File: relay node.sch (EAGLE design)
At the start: 25 parts, among them J1 Channels, J2 LED, J3 PROG, J4 AUX, U1 ESP-WROOM-02U, U2 MCP23018-E/SS, U3 TLV75533

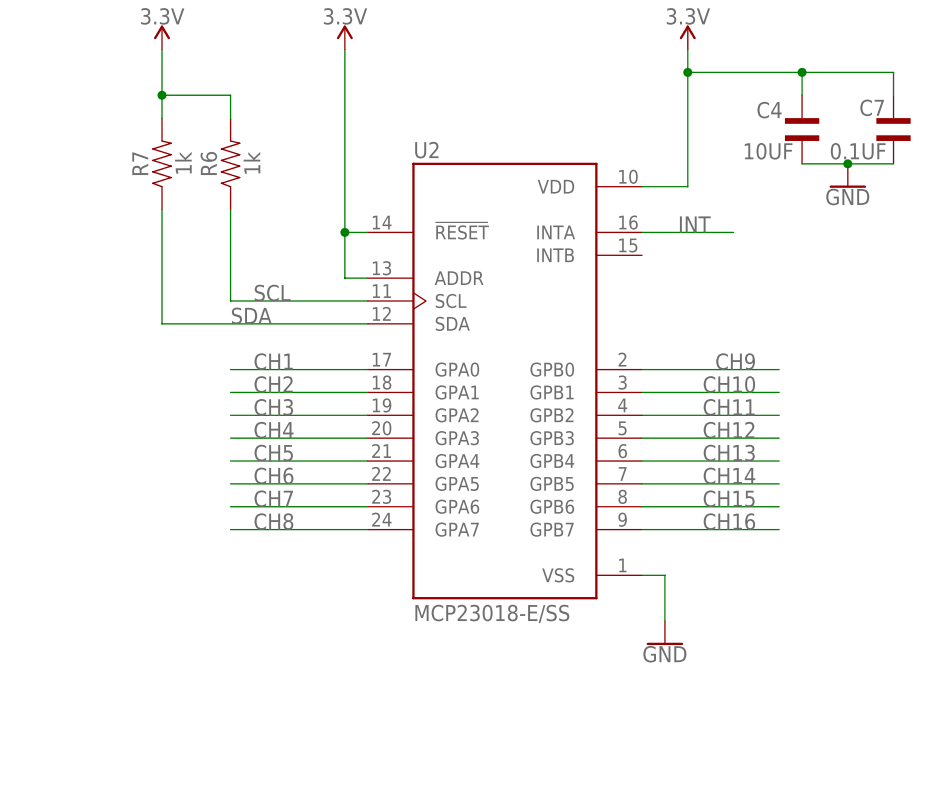
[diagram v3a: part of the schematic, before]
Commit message: Replace I/O expander to MCP23018 28-SOIC Replace BOM part numbers to match JLCPB inventory
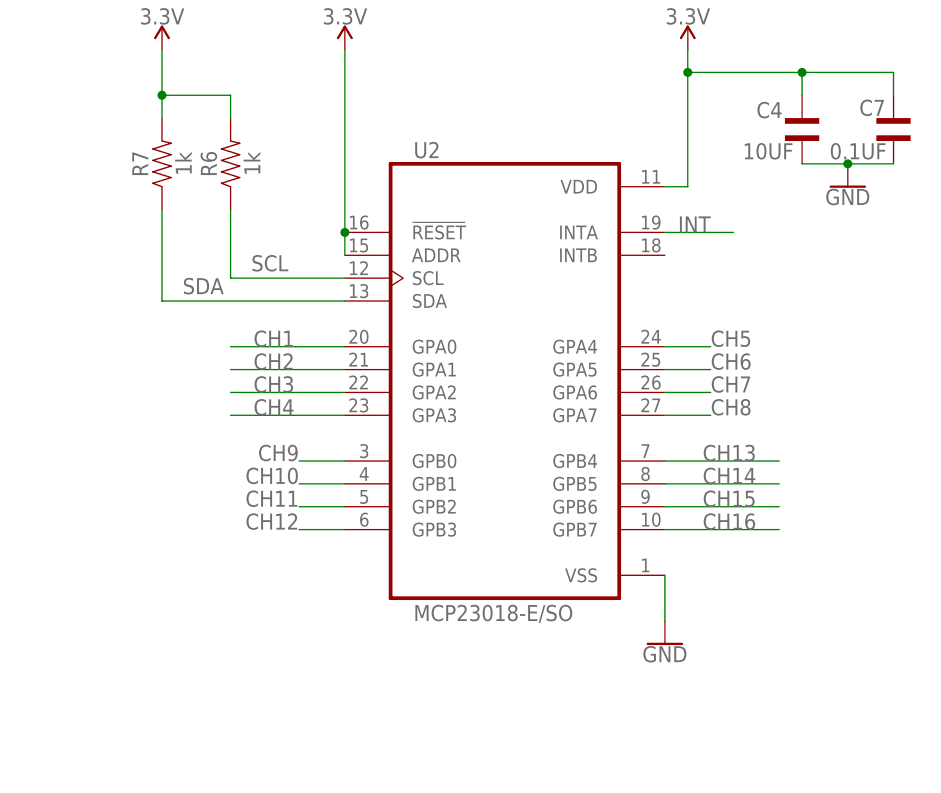
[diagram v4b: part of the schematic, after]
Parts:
- U2: value MCP23018-E/SS -> MCP23018-E/SO; device SFM-Project:MCP23018-E/SS -> SFM-Project:MCP23018-E/SO
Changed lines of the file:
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@@
 <part name="R7" library="SFM-Project" deviceset="1KOHM" device="-0603-1/10W-5%" value="1k"/>
 <part name="SUPPLY6" library="SparkFun-PowerSymbols" deviceset="3.3V" device=""/>
-<part name="U2" library="SFM-Project" deviceset="MCP23018-E/SS" device=""/>
+<part name="U2" library="SFM-Project" deviceset="MCP23018-E/SO" device=""/>
 <part name="SUPPLY7" library="SparkFun-PowerSymbols" deviceset="3.3V" device=""/>
 <part name="U1" library="SFM-Project" deviceset="ESP-WROOM-02U" device=""/>
@@
 <wire x1="180.34" y1="154.94" x2="180.34" y2="152.4" width="0.1524" layer="91"/>
 <wire x1="180.34" y1="152.4" x2="180.34" y2="139.7" width="0.1524" layer="91"/>
-<wire x1="180.34" y1="139.7" x2="175.26" y2="139.7" width="0.1524" layer="91"/>
+<wire x1="180.34" y1="139.7" x2="177.8" y2="139.7" width="0.1524" layer="91"/>
 <pinref part="C4" gate="G$1" pin="1"/>
 <wire x1="193.04" y1="149.86" x2="193.04" y2="152.4" width="0.1524" layer="91"/>
@@
 <pinref part="U2" gate="G$1" pin="ADDR"/>
 <pinref part="SUPPLY7" gate="G$1" pin="3.3V"/>
-<wire x1="144.78" y1="129.54" x2="142.24" y2="129.54" width="0.1524" layer="91"/>
-<wire x1="142.24" y1="129.54" x2="142.24" y2="134.62" width="0.1524" layer="91"/>
+<wire x1="142.24" y1="132.08" x2="142.24" y2="134.62" width="0.1524" layer="91"/>
 <pinref part="U2" gate="G$1" pin="!RESET"/>
 <wire x1="142.24" y1="134.62" x2="142.24" y2="154.94" width="0.1524" layer="91"/>
-<wire x1="144.78" y1="134.62" x2="142.24" y2="134.62" width="0.1524" layer="91"/>
 <junction x="142.24" y="134.62"/>
 </segment>
@@
 <pinref part="U2" gate="G$1" pin="VSS"/>
 <pinref part="GND4" gate="1" pin="GND"/>
-<wire x1="175.26" y1="96.52" x2="177.8" y2="96.52" width="0.1524" layer="91"/>
 <wire x1="177.8" y1="96.52" x2="177.8" y2="91.44" width="0.1524" layer="91"/>
 </segment>
@@
 <segment>
 <pinref part="U2" gate="G$1" pin="GPA0"/>
-<wire x1="144.78" y1="119.38" x2="129.54" y2="119.38" width="0.1524" layer="91"/>
-<label x="132.08" y="119.38" size="1.778" layer="95"/>
+<wire x1="142.24" y1="121.92" x2="129.54" y2="121.92" width="0.1524" layer="91"/>
+<label x="132.08" y="121.92" size="1.778" layer="95"/>
 </segment>
 <segment>
@@
 <segment>
 <pinref part="U2" gate="G$1" pin="GPA1"/>
-<wire x1="144.78" y1="116.84" x2="129.54" y2="116.84" width="0.1524" layer="91"/>
-<label x="132.08" y="116.84" size="1.778" layer="95"/>
+<wire x1="142.24" y1="119.38" x2="129.54" y2="119.38" width="0.1524" layer="91"/>
+<label x="132.08" y="119.38" size="1.778" layer="95"/>
 </segment>
 <segment>
@@
 <segment>
 <pinref part="U2" gate="G$1" pin="GPA2"/>
-<wire x1="144.78" y1="114.3" x2="129.54" y2="114.3" width="0.1524" layer="91"/>
-<label x="132.08" y="114.3" size="1.778" layer="95"/>
+<wire x1="142.24" y1="116.84" x2="129.54" y2="116.84" width="0.1524" layer="91"/>
+<label x="132.08" y="116.84" size="1.778" layer="95"/>
 </segment>
 <segment>
@@
 <segment>
 <pinref part="U2" gate="G$1" pin="GPA3"/>
-<wire x1="144.78" y1="111.76" x2="129.54" y2="111.76" width="0.1524" layer="91"/>
-<label x="132.08" y="111.76" size="1.778" layer="95"/>
+<wire x1="142.24" y1="114.3" x2="129.54" y2="114.3" width="0.1524" layer="91"/>
+<label x="132.08" y="114.3" size="1.778" layer="95"/>
 </segment>
 <segment>
@@
 <segment>
 <pinref part="U2" gate="G$1" pin="GPA4"/>
-<wire x1="144.78" y1="109.22" x2="129.54" y2="109.22" width="0.1524" layer="91"/>
-<label x="132.08" y="109.22" size="1.778" layer="95"/>
+<wire x1="177.8" y1="121.92" x2="182.88" y2="121.92" width="0.1524" layer="91"/>
+<label x="182.88" y="121.92" size="1.778" layer="95"/>
 </segment>
 <segment>
@@
 <segment>
 <pinref part="U2" gate="G$1" pin="GPA5"/>
-<wire x1="144.78" y1="106.68" x2="129.54" y2="106.68" width="0.1524" layer="91"/>
-<label x="132.08" y="106.68" size="1.778" layer="95"/>
+<wire x1="177.8" y1="119.38" x2="182.88" y2="119.38" width="0.1524" layer="91"/>
+<label x="182.88" y="119.38" size="1.778" layer="95"/>
 </segment>
 <segment>
@@
 <segment>
 <pinref part="U2" gate="G$1" pin="GPA6"/>
-<wire x1="144.78" y1="104.14" x2="129.54" y2="104.14" width="0.1524" layer="91"/>
-<label x="132.08" y="104.14" size="1.778" layer="95"/>
+<wire x1="177.8" y1="116.84" x2="182.88" y2="116.84" width="0.1524" layer="91"/>
+<label x="182.88" y="116.84" size="1.778" layer="95"/>
 </segment>
 <segment>
@@
 <segment>
 <pinref part="U2" gate="G$1" pin="GPA7"/>
-<wire x1="144.78" y1="101.6" x2="129.54" y2="101.6" width="0.1524" layer="91"/>
-<label x="132.08" y="101.6" size="1.778" layer="95"/>
+<wire x1="177.8" y1="114.3" x2="182.88" y2="114.3" width="0.1524" layer="91"/>
+<label x="182.88" y="114.3" size="1.778" layer="95"/>
 </segment>
 <segment>
@@
 <segment>
 <pinref part="U2" gate="G$1" pin="GPB0"/>
-<wire x1="175.26" y1="119.38" x2="190.5" y2="119.38" width="0.1524" layer="91"/>
-<label x="187.96" y="119.38" size="1.778" layer="95" align="bottom-right"/>
+<wire x1="142.24" y1="109.22" x2="137.16" y2="109.22" width="0.1524" layer="91"/>
+<label x="137.16" y="109.22" size="1.778" layer="95" align="bottom-right"/>
 </segment>
 <segment>
@@
 <segment>
 <pinref part="U2" gate="G$1" pin="GPB1"/>
-<wire x1="175.26" y1="116.84" x2="190.5" y2="116.84" width="0.1524" layer="91"/>
-<label x="187.96" y="116.84" size="1.778" layer="95" align="bottom-right"/>
+<wire x1="142.24" y1="106.68" x2="137.16" y2="106.68" width="0.1524" layer="91"/>
+<label x="137.16" y="106.68" size="1.778" layer="95" align="bottom-right"/>
 </segment>
 <segment>
@@
 <segment>
 <pinref part="U2" gate="G$1" pin="GPB2"/>
-<wire x1="175.26" y1="114.3" x2="190.5" y2="114.3" width="0.1524" layer="91"/>
-<label x="187.96" y="114.3" size="1.778" layer="95" align="bottom-right"/>
+<wire x1="142.24" y1="104.14" x2="137.16" y2="104.14" width="0.1524" layer="91"/>
+<label x="137.16" y="104.14" size="1.778" layer="95" align="bottom-right"/>
 </segment>
 <segment>
@@
 <segment>
 <pinref part="U2" gate="G$1" pin="GPB3"/>
-<wire x1="175.26" y1="111.76" x2="190.5" y2="111.76" width="0.1524" layer="91"/>
-<label x="187.96" y="111.76" size="1.778" layer="95" align="bottom-right"/>
+<wire x1="142.24" y1="101.6" x2="137.16" y2="101.6" width="0.1524" layer="91"/>
+<label x="137.16" y="101.6" size="1.778" layer="95" align="bottom-right"/>
 </segment>
 <segment>
@@
 <segment>
 <pinref part="U2" gate="G$1" pin="GPB4"/>
-<wire x1="175.26" y1="109.22" x2="190.5" y2="109.22" width="0.1524" layer="91"/>
+<wire x1="177.8" y1="109.22" x2="190.5" y2="109.22" width="0.1524" layer="91"/>
 <label x="187.96" y="109.22" size="1.778" layer="95" align="bottom-right"/>
 </segment>
@@
 <segment>
 <pinref part="U2" gate="G$1" pin="GPB5"/>
-<wire x1="175.26" y1="106.68" x2="190.5" y2="106.68" width="0.1524" layer="91"/>
+<wire x1="177.8" y1="106.68" x2="190.5" y2="106.68" width="0.1524" layer="91"/>
 <label x="187.96" y="106.68" size="1.778" layer="95" align="bottom-right"/>
 </segment>
@@
 <segment>
 <pinref part="U2" gate="G$1" pin="GPB6"/>
-<wire x1="175.26" y1="104.14" x2="190.5" y2="104.14" width="0.1524" layer="91"/>
+<wire x1="177.8" y1="104.14" x2="190.5" y2="104.14" width="0.1524" layer="91"/>
 <label x="187.96" y="104.14" size="1.778" layer="95" align="bottom-right"/>
 </segment>
@@
 <segment>
 <pinref part="U2" gate="G$1" pin="GPB7"/>
-<wire x1="175.26" y1="101.6" x2="190.5" y2="101.6" width="0.1524" layer="91"/>
+<wire x1="177.8" y1="101.6" x2="190.5" y2="101.6" width="0.1524" layer="91"/>
 <label x="187.96" y="101.6" size="1.778" layer="95" align="bottom-right"/>
 </segment>
@@
 </segment>
 <segment>
-<wire x1="144.78" y1="124.46" x2="121.92" y2="124.46" width="0.1524" layer="91"/>
+<wire x1="142.24" y1="127" x2="121.92" y2="127" width="0.1524" layer="91"/>
 <pinref part="R7" gate="G$1" pin="1"/>
-<wire x1="121.92" y1="124.46" x2="121.92" y2="137.16" width="0.1524" layer="91"/>
-<label x="129.54" y="124.46" size="1.778" layer="95"/>
+<wire x1="121.92" y1="127" x2="121.92" y2="137.16" width="0.1524" layer="91"/>
+<label x="124.206" y="127.762" size="1.778" layer="95"/>
 <pinref part="U2" gate="G$1" pin="SDA"/>
 </segment>
@@
 <pinref part="R6" gate="G$1" pin="1"/>
 <pinref part="U2" gate="G$1" pin="SCL"/>
-<wire x1="129.54" y1="137.16" x2="129.54" y2="127" width="0.1524" layer="91"/>
-<wire x1="129.54" y1="127" x2="144.78" y2="127" width="0.1524" layer="91"/>
-<label x="132.08" y="127" size="1.778" layer="95"/>
+<wire x1="129.54" y1="137.16" x2="129.54" y2="129.54" width="0.1524" layer="91"/>
+<wire x1="129.54" y1="129.54" x2="142.24" y2="129.54" width="0.1524" layer="91"/>
+<label x="131.826" y="130.302" size="1.778" layer="95"/>
 </segment>
 <segment>
@@
 <segment>
 <pinref part="U2" gate="G$1" pin="INTA"/>
-<wire x1="175.26" y1="134.62" x2="185.42" y2="134.62" width="0.1524" layer="91"/>
+<wire x1="177.8" y1="134.62" x2="185.42" y2="134.62" width="0.1524" layer="91"/>
 <label x="182.88" y="134.62" size="1.778" layer="95" align="bottom-right"/>
 </segment>

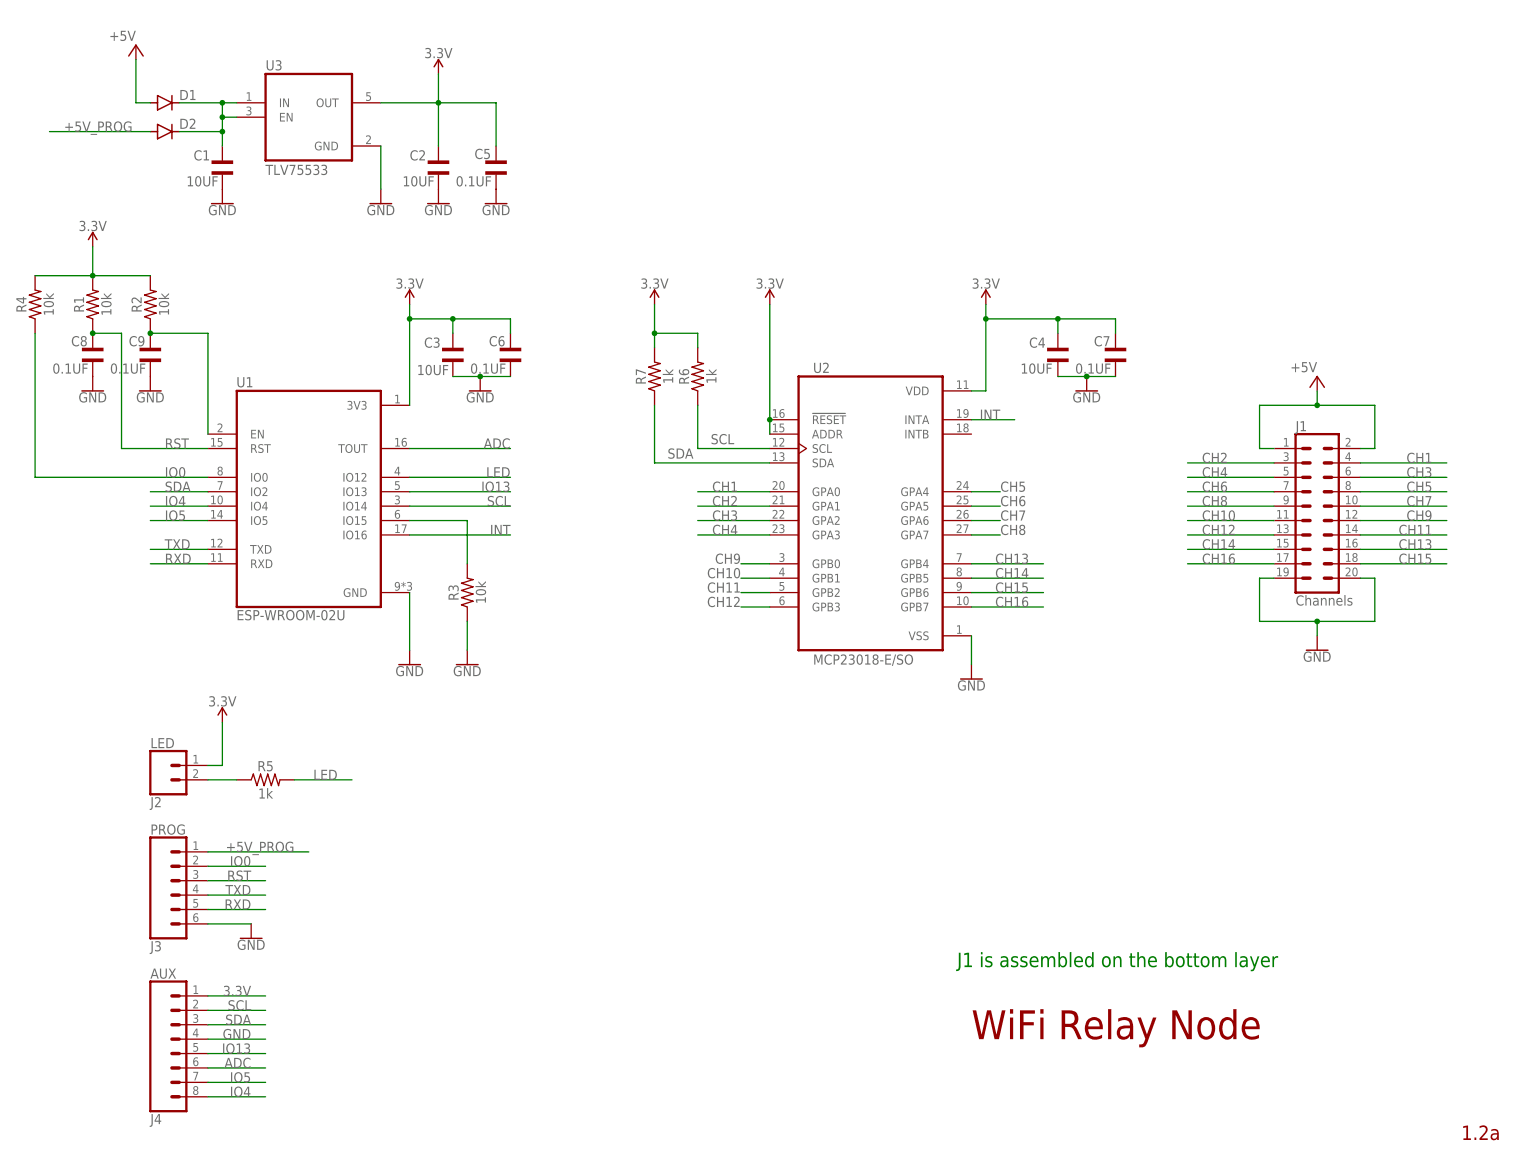
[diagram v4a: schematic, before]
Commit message: Replace volt regulator
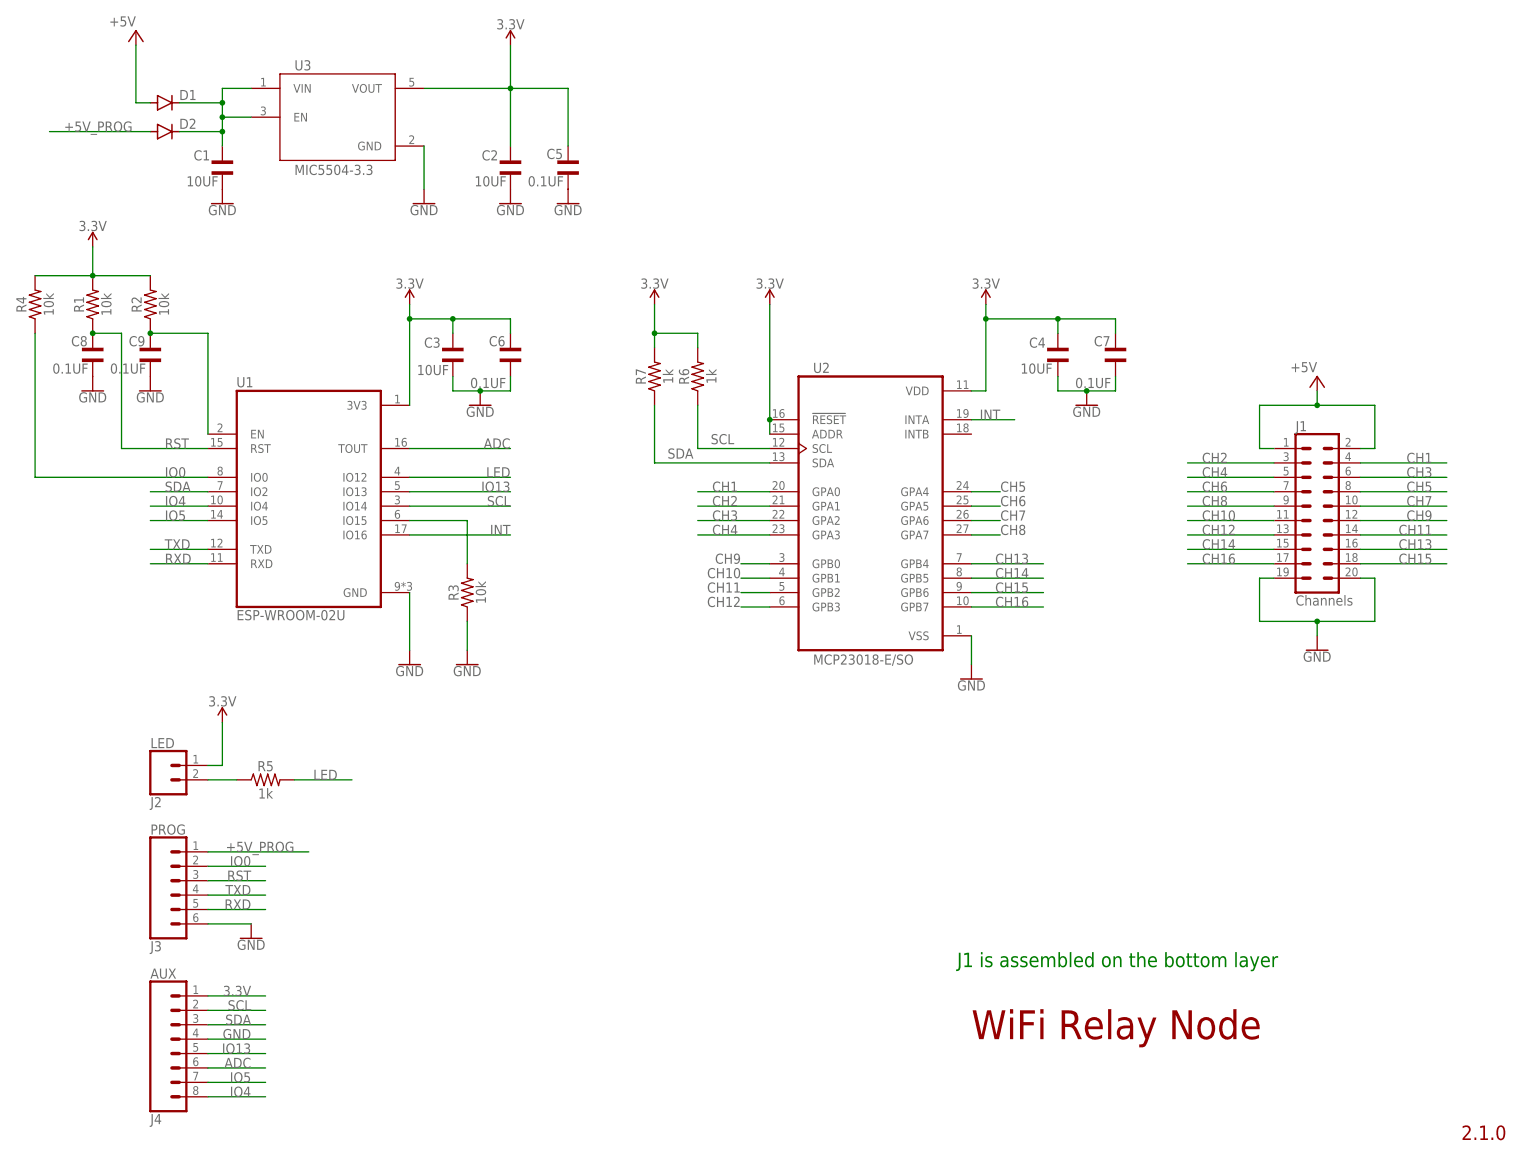
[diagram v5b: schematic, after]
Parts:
- U3: value TLV75533 -> MIC5504-3.3; device SFM-Project:TLV75533PDBVR -> SFM-Project:MIC5504-3.3YM5-T5
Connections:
- net 3.3V: now also U3.VOUT; no longer U3.OUT
- net N$1: now also U3.VIN; no longer U3.IN
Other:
- note added: "2.1.0"
- note removed: "1.2a"
- moved on the sheet: C2, C5, U3

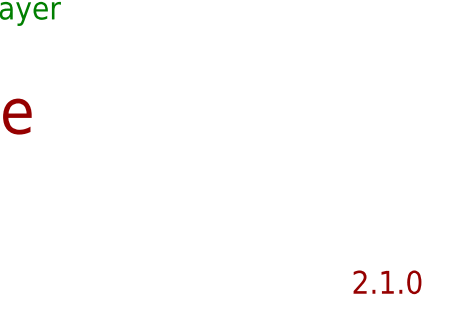
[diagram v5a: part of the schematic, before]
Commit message: Minor changes for production PCB ordered -  v1.0.0
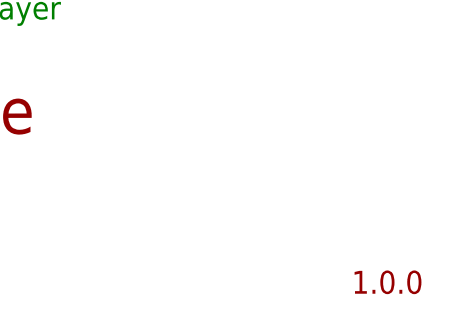
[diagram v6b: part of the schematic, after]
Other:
- note added: "1.0.0"
- note removed: "2.1.0"
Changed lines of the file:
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@@
 <sheet>
 <plain>
-<text x="264.16" y="7.62" size="2.54" layer="94" font="vector" ratio="7" distance="3">2.1.0</text>
+<text x="264.16" y="7.62" size="2.54" layer="94" font="vector" ratio="7" distance="3">1.0.0</text>
 <text x="177.8" y="25.4" size="5.08" layer="94" font="vector" ratio="7" distance="3">WiFi Relay Node</text>
 <text x="175.26" y="38.1" size="2.54" layer="91">J1 is assembled on the bottom layer</text>
